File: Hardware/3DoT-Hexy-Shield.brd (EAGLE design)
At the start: 100 x 80 mm, 0 parts

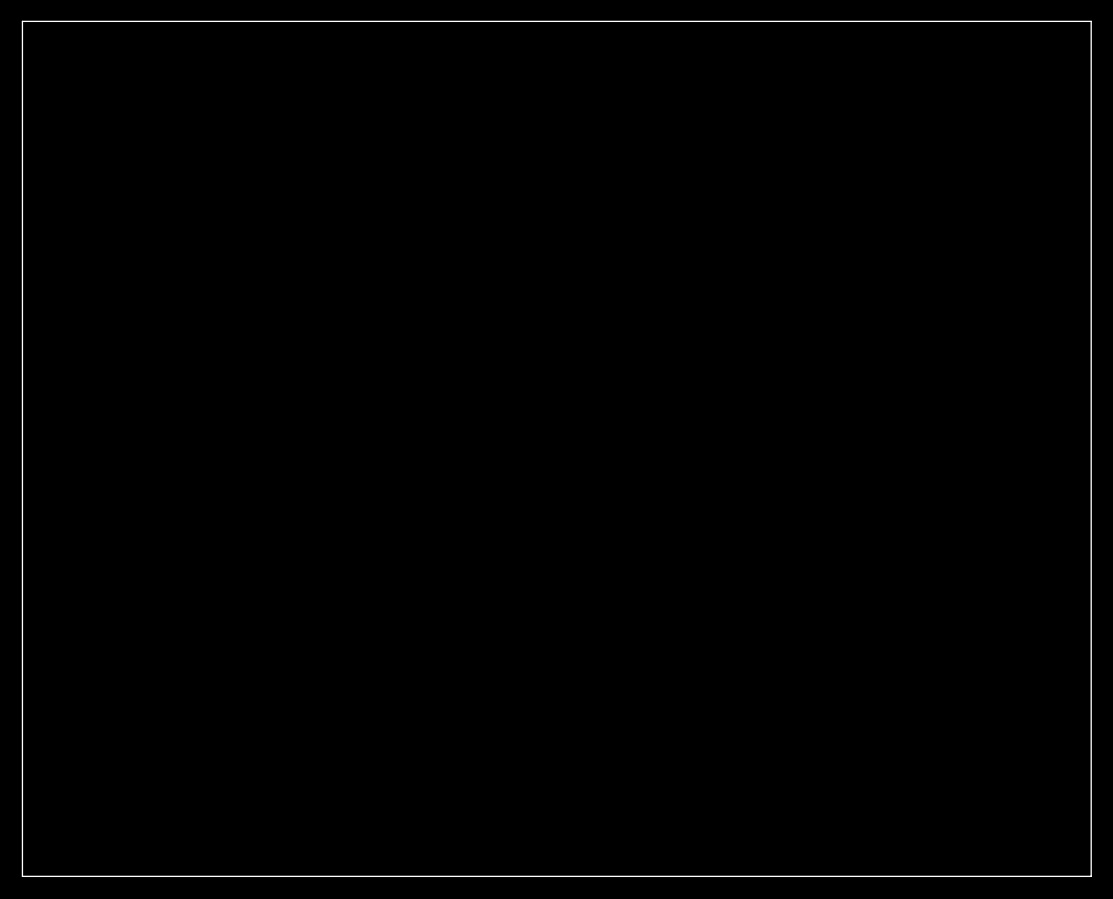
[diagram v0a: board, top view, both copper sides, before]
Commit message: Finished board layout for the shield
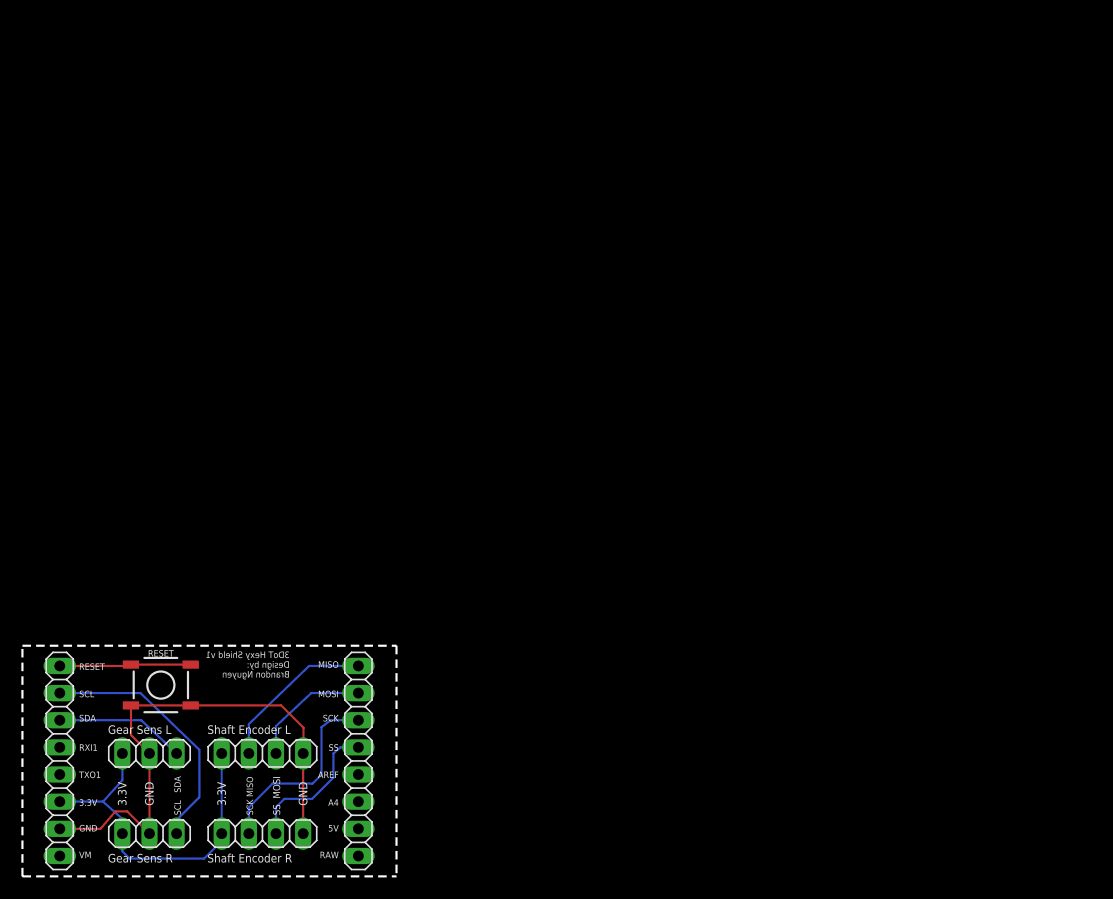
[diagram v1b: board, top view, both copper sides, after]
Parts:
- added JP1, JP2: (no value), pinhead:1X08
- added JP3, JP4: (no value), pinhead:1X04
- added JP5, JP6: (no value), pinhead:1X03
- added RESET: (no value), SparkFun-Switches:TACTILE_SWITCH_SMD_5.2MM
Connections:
- new net 3.3V: JP2.6, JP3.1, JP4.1, JP5.1, JP6.1
- new net 5V: JP1.7
- new net A4: JP1.6
- new net AREF: JP1.5
- new net GND: JP2.7, JP3.4, JP4.4, JP5.2, JP6.2, RESET.3, RESET.4
- new net MISO: JP1.1, JP4.2
- new net MOSI: JP1.2, JP4.3
- new net RAW: JP1.8
- new net RESET: JP2.1, RESET.1, RESET.2
- new net RXI1: JP2.4
- new net SCK: JP1.3, JP3.2
- new net SCL: JP2.2, JP5.3
- new net SDA: JP2.3, JP6.3
- new net SS: JP1.4, JP3.3
- new net TXO1: JP2.5
- new net VM: JP2.8
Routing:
- net GND: track 0.00 -> 49.6 mm
- net 3.3V: track 0.00 -> 33.2 mm
- net SCL: track 0.00 -> 23.9 mm
- net SCK: track 0.00 -> 18.6 mm
- net MISO: track 0.00 -> 15.2 mm
- net SS: track 0.00 -> 13.8 mm
- net RESET: track 0.00 -> 12.4 mm
- net SDA: track 0.00 -> 12.2 mm
- net MOSI: track 0.00 -> 11.5 mm
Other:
- board size 100 x 80 mm -> 35 x 21.6 mm
- board text added: "3.3V"
- board text added: "3DoT Hexy Shield v1 Design by: Brandon Nguyen"
- board text added: "5V"
- board text added: "A4"
- board text added: "AREF"
- board text added: "GND"
- board text added: "Gear Sens L"
- board text added: "Gear Sens R"
- board text added: "MISO"
- board text added: "MOSI"
- board text added: "RAW"
- board text added: "RESET"
- board text added: "RXI1"
- board text added: "SCK"
- board text added: "SCK MISO"
- board text added: "SCL"
- board text added: "SCL SDA"
- board text added: "SDA"
- board text added: "SS"
- board text added: "SS MOSI"
- board text added: "Shaft Encoder L"
- board text added: "Shaft Encoder R"
- board text added: "TXO1"
- board text added: "VM"
